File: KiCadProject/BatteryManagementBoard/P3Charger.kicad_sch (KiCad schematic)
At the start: 58 parts, among them Q301 NFET_Gatenames, Q302 NFET_Gatenames, Q303 NFET_Gatenames, Q304 NFET_Gatenames, Q305 PMOS_Gatenames, U301 BQ25713

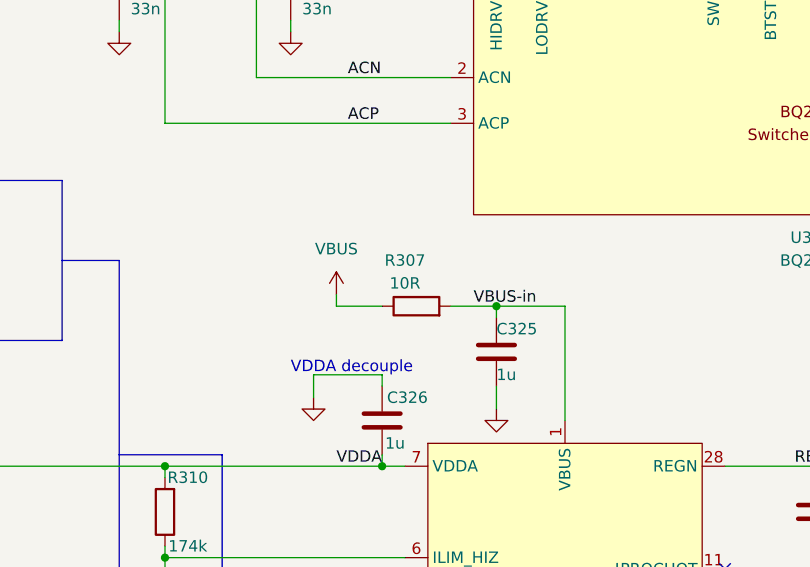
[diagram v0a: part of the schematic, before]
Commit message: Components selected, MfID added to schematics, and components ordered
Signed-off-by: Eldalote.Electronics <Eldalote.Electronics@gmail.com>
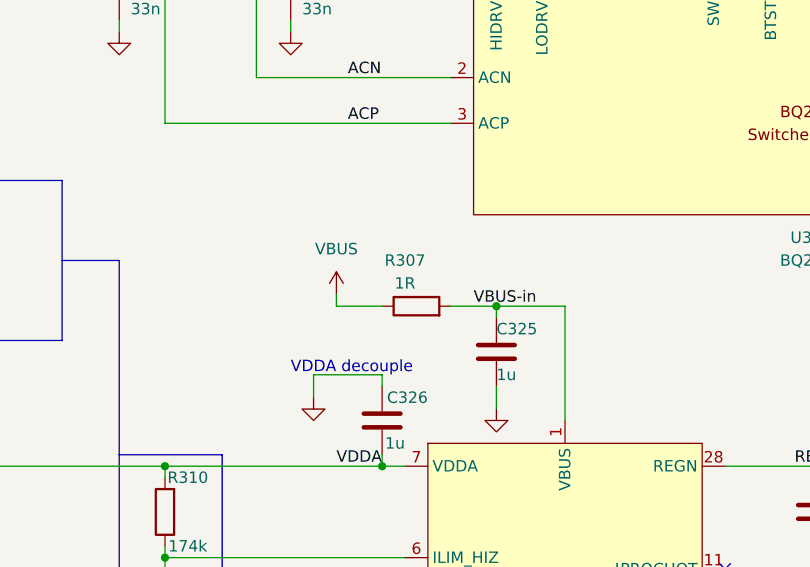
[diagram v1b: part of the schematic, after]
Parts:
- C301, C302, C303, C304, C305, C306, C307, C314, C315, C317, C318, C319, C320, C321, C324: Extra Requirement (none) -> 25V; MfID (none) -> CL21A106KAYNNNG
- C308, C309: Extra Requirement (none) -> 25V; MfID (none) -> 885012205053
- C310: Extra Requirement (none) -> 25V; MfID (none) -> CL05B103KB5NNNC
- C311: Extra Requirement (none) -> 25V; MfID (none) -> 885012205061
- C312, C313: Extra Requirement (none) -> 25V; MfID (none) -> GRM155R71H473KE14D
- C316: footprint Capacitor_SMD:C_0603_1608Metric -> Capacitor_SMD:C_0805_2012Metric; Extra Requirement (none) -> 25V; MfID (none) -> CL21A106KAYNNNG
- C322, C325, C326: Extra Requirement (none) -> 25V; MfID (none) -> CL10A105KA8NNNC
- C323: Extra Requirement (none) -> 25V; MfID (none) -> CL05A104KA5NNNC
- C327: MfID (none) -> 885012005058
- C328: MfID (none) -> GCM155R71H182KA37D
- C329: MfID (none) -> 885012005056
- C330: MfID (none) -> 885012205060
- C331: Extra Requirement (none) -> 10V; MfID (none) -> CL10A225KO8NNNC
- C332, C333: MfID (none) -> 885012205055
- L301: MfID (none) -> SRP1265C-2R2M
- Q301, Q302, Q303, Q304: MfID (none) -> AON7400A
- Q305: MfID (none) -> DMP3011SFVW-13
- R301, R304: MfID (none) -> D1MPC1206QR010FF-T5
- R302, R303: MfID (none) -> RC0402FR-074R99L
- R305, R306, R308: MfID (none) -> RK73H1ETTP10R0F
- R307: value 10R -> 1R; footprint Resistor_SMD:R_0402_1005Metric -> Resistor_SMD:R_0603_1608Metric; MfID (none) -> RMCF0603FT1R00
- R309, R312, R313: MfID (none) -> CR0402-FX-1003GLF
- R310: MfID (none) -> RMCF0402FT174K
- R311: MfID (none) -> CR0402-FX-3003GLF
- R314: MfID (none) -> CR0402-FX-4022GLF
- R315, R316, R317: MfID (none) -> CR0402-FX-1002GLF
- R318: MfID (none) -> RMCF0402FT137K
- U301: MfID (none) -> BQ25713BRSNR

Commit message: Layout on the battery management board
Signed-off-by: Eldalote.Electronics <Eldalote.Electronics@gmail.com>
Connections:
- net ILIM_HIZ: now reaches R310.1, R312.2, U301.6 (ILIM_HIZ)
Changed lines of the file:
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@@
     (effects (font (size 1.27 1.27)) (justify right bottom))
+  )
+  (label "ILIM_HIZ" (at 88.9 130.81 0)
+    (effects (font (size 1.27 1.27)) (justify left bottom))
   )
   (label "BQ_EN_OTG" (at 250.19 115.57 180)

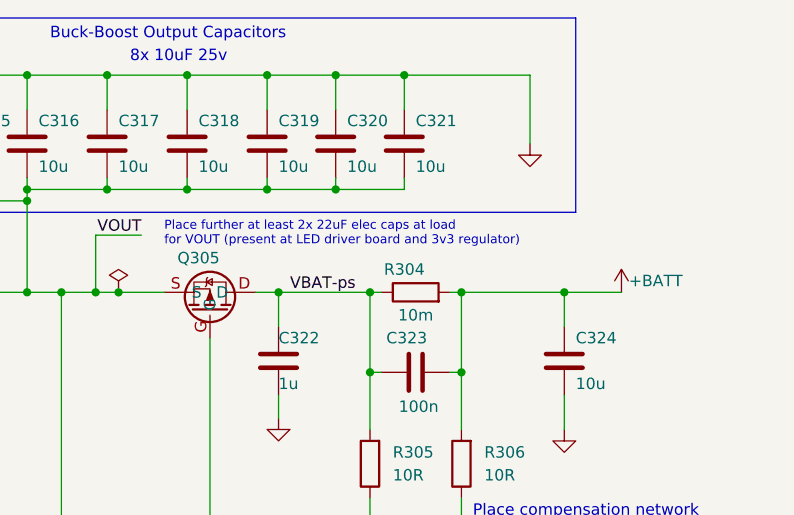
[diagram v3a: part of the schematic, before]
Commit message: Made ready to order PCBs. Some problems with ordering due to misunderstanding. Thinking about solutions
Signed-off-by: Eldalote.Electronics <Eldalote.Electronics@gmail.com>
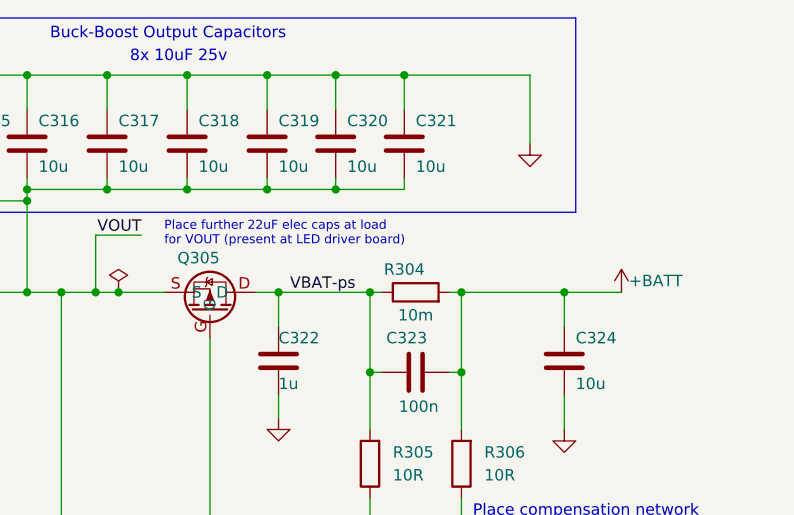
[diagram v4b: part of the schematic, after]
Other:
- note added: "Place further 22uF elec caps at load for VOUT (present at LED driver board)"
- note removed: "Place further at least 2x 22uF elec caps at load for VOUT (present at LED driver board and 3v3 regulator)"
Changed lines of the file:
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@@
     (effects (font (size 1.27 1.27)) (justify left bottom))
   )
-  (text "Place further at least 2x 22uF elec caps at load\nfor VOUT (present at LED driver board and 3v3 regulator)"
+  (text "Place further 22uF elec caps at load\nfor VOUT (present at LED driver board)"
     (at 215.9 38.1 0)
     (effects (font (size 1 1)) (justify left bottom))
